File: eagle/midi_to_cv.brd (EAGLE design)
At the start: 100.1 x 82 mm, 67 parts, among them IC1 TL082P, IC2 TL084P, IC4 TL082P, IC6 TL082P, IC7 TL082P, U1 ATMEGA328P_PDIP, U2 MCP4822-E/P, U3 MCP4822-E/P, U4 MCP4822-E/P, U5 MCP4822-E/P

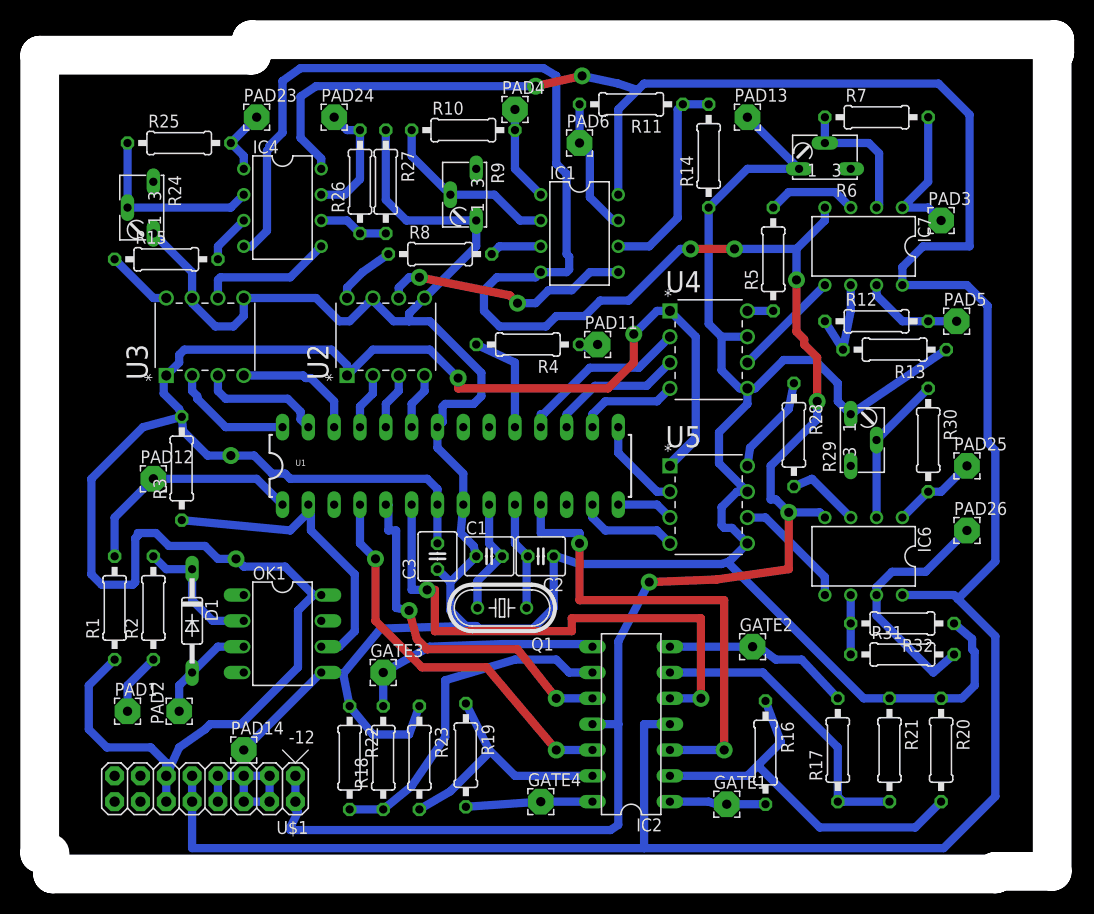
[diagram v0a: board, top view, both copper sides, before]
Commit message: updated arduino code
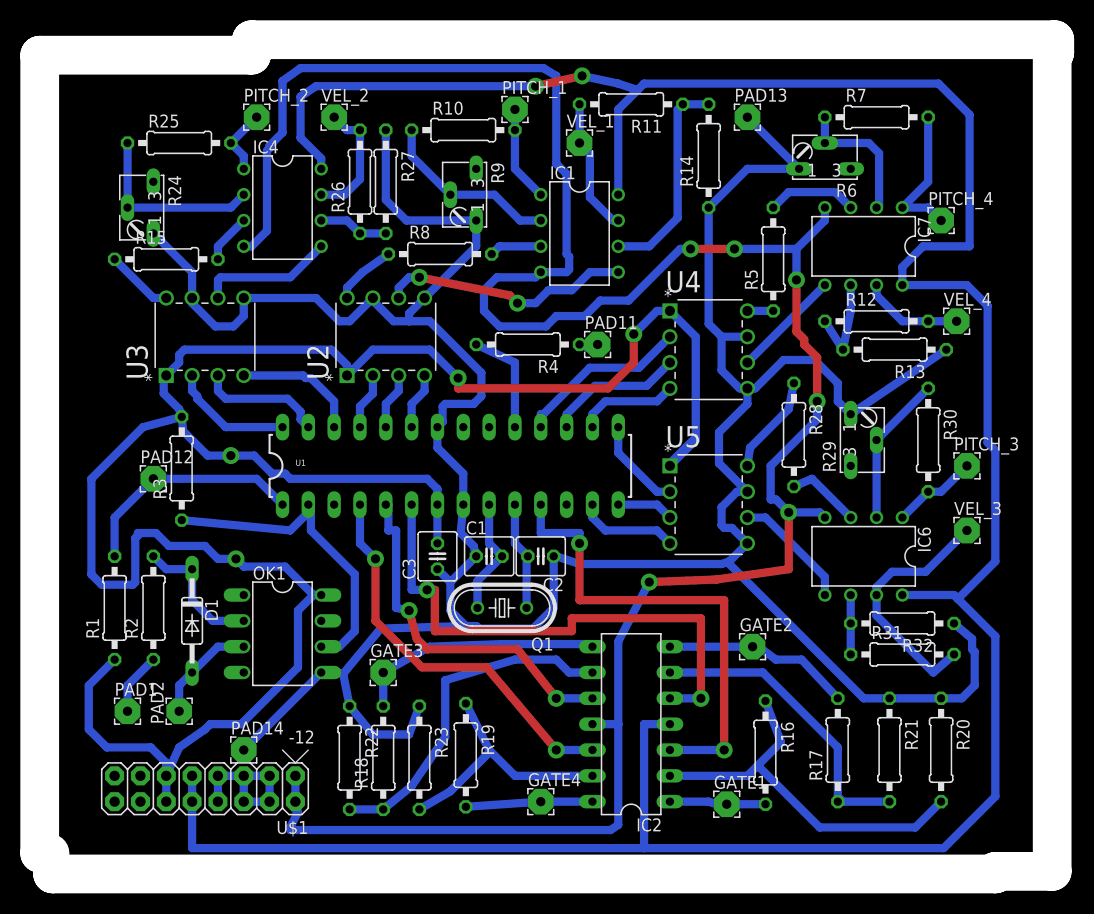
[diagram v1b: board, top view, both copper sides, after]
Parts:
- PITCH_1, PITCH_2, PITCH_3, PITCH_4: value pitch cv -> (none)
- VEL_1, VEL_2, VEL_3, VEL_4: value velocity cv -> (none)
- renumbered PAD23 to PITCH_2, PAD24 to VEL_2, PAD25 to PITCH_3, PAD26 to VEL_3, PAD3 to PITCH_4, PAD4 to PITCH_1, PAD5 to VEL_4, PAD6 to VEL_1
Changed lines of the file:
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@@
 <element name="R5" library="rcl" package="0207/10" value="3.3k" x="72.39" y="59.69" rot="R90"/>
 <element name="R6" library="pot" package="B64W" value="10k" x="77.47" y="68.58" rot="R180"/>
-<element name="PAD3" library="wirepad" package="2,54/0,9" value="pitch cv" x="88.9" y="63.5"/>
+<element name="PITCH_4" library="wirepad" package="2,54/0,9" value="" x="88.9" y="63.5"/>
 <element name="R7" library="rcl" package="0207/10" value="5k" x="82.55" y="73.66"/>
 <element name="R12" library="rcl" package="0207/10" value="1k" x="82.55" y="53.594"/>
 <element name="R13" library="rcl" package="0207/10" value="1k" x="84.328" y="50.8" rot="R180"/>
-<element name="PAD5" library="wirepad" package="2,54/0,9" value="velocity cv" x="90.424" y="53.594"/>
+<element name="VEL_4" library="wirepad" package="2,54/0,9" value="" x="90.424" y="53.594"/>
 <element name="U4" library="MCP4822" package="DIP254P762X432-8" value="MCP4822-E/P" x="69.85" y="46.99">
 <attribute name="PACKAGE" value="DIP-8" x="69.85" y="46.99" size="1.778" layer="27" display="off"/>
@@
 <element name="R8" library="rcl" package="0207/10" value="3.3k" x="39.624" y="60.198"/>
 <element name="R9" library="pot" package="B64W" value="10k" x="43.18" y="66.04" rot="R270"/>
-<element name="PAD4" library="wirepad" package="2,54/0,9" value="pitch cv" x="46.99" y="74.422"/>
+<element name="PITCH_1" library="wirepad" package="2,54/0,9" value="" x="46.99" y="74.422"/>
 <element name="R10" library="rcl" package="0207/10" value="5k" x="41.91" y="72.39"/>
 <element name="R11" library="rcl" package="0207/10" value="1k" x="58.42" y="74.93" rot="R180"/>
 <element name="R14" library="rcl" package="0207/10" value="1k" x="66.04" y="69.85" rot="R90"/>
-<element name="PAD6" library="wirepad" package="2,54/0,9" value="velocity cv" x="53.34" y="71.12"/>
+<element name="VEL_1" library="wirepad" package="2,54/0,9" value="" x="53.34" y="71.12"/>
 <element name="U2" library="MCP4822" package="DIP254P762X432-8" value="MCP4822-E/P" x="38.1" y="55.88" rot="R90">
 <attribute name="PACKAGE" value="DIP-8" x="72.39" y="41.91" size="1.778" layer="27" rot="R90" display="off"/>
@@
 <element name="R15" library="rcl" package="0207/10" value="3.3k" x="12.7" y="59.69"/>
 <element name="R24" library="pot" package="B64W" value="10k" x="11.43" y="64.77" rot="R270"/>
-<element name="PAD23" library="wirepad" package="2,54/0,9" value="pitch cv" x="21.59" y="73.66"/>
+<element name="PITCH_2" library="wirepad" package="2,54/0,9" value="" x="21.59" y="73.66"/>
 <element name="R25" library="rcl" package="0207/10" value="5k" x="13.97" y="71.12"/>
 <element name="R26" library="rcl" package="0207/10" value="1k" x="31.75" y="67.31" rot="R90"/>
 <element name="R27" library="rcl" package="0207/10" value="1k" x="34.29" y="67.31" rot="R270"/>
-<element name="PAD24" library="wirepad" package="2,54/0,9" value="velocity cv" x="29.21" y="73.66"/>
+<element name="VEL_2" library="wirepad" package="2,54/0,9" value="" x="29.21" y="73.66"/>
 <element name="U3" library="MCP4822" package="DIP254P762X432-8" value="MCP4822-E/P" x="20.32" y="55.88" rot="R90">
 <attribute name="PACKAGE" value="DIP-8" x="54.61" y="41.91" size="1.778" layer="27" rot="R90" display="off"/>
@@
 <element name="R28" library="rcl" package="0207/10" value="3.3k" x="74.422" y="42.418" rot="R270"/>
 <element name="R29" library="pot" package="B64W" value="10k" x="80.01" y="41.91" rot="R90"/>
-<element name="PAD25" library="wirepad" package="2,54/0,9" value="pitch cv" x="91.44" y="39.37"/>
+<element name="PITCH_3" library="wirepad" package="2,54/0,9" value="" x="91.44" y="39.37"/>
 <element name="R30" library="rcl" package="0207/10" value="5k" x="87.63" y="41.91" rot="R270"/>
 <element name="R31" library="rcl" package="0207/10" value="1k" x="85.09" y="20.828"/>
 <element name="R32" library="rcl" package="0207/10" value="1k" x="85.09" y="23.876" rot="R180"/>
-<element name="PAD26" library="wirepad" package="2,54/0,9" value="velocity cv" x="91.44" y="33.02"/>
+<element name="VEL_3" library="wirepad" package="2,54/0,9" value="" x="91.44" y="33.02"/>
 <element name="U5" library="MCP4822" package="DIP254P762X432-8" value="MCP4822-E/P" x="69.85" y="31.75">
 <attribute name="PACKAGE" value="DIP-8" x="55.88" y="-2.54" size="1.778" layer="27" display="off"/>
@@
 </signal>
 <signal name="N$9">
-<contactref element="PAD3" pad="1"/>
+<contactref element="PITCH_4" pad="1"/>
 <contactref element="R7" pad="2"/>
 <contactref element="IC7" pad="1"/>
@@
 <signal name="N$19">
 <contactref element="R12" pad="2"/>
-<contactref element="PAD5" pad="1"/>
+<contactref element="VEL_4" pad="1"/>
 <contactref element="IC7" pad="7"/>
 <wire x1="82.55" y1="57.15" x2="82.55" y2="56.134" width="0.8128" layer="16"/>
@@
 </signal>
 <signal name="N$17">
-<contactref element="PAD4" pad="1"/>
+<contactref element="PITCH_1" pad="1"/>
 <contactref element="R10" pad="2"/>
 <contactref element="IC1" pad="1"/>
@@
 <signal name="N$21">
 <contactref element="R11" pad="2"/>
-<contactref element="PAD6" pad="1"/>
+<contactref element="VEL_1" pad="1"/>
 <contactref element="IC1" pad="7"/>
 <wire x1="57.15" y1="63.5" x2="56.642" y2="63.5" width="0.8128" layer="16"/>
@@
 </signal>
 <signal name="N$49">
-<contactref element="PAD23" pad="1"/>
+<contactref element="PITCH_2" pad="1"/>
 <contactref element="R25" pad="2"/>
 <contactref element="IC4" pad="1"/>
@@
 <signal name="N$52">
 <contactref element="R26" pad="2"/>
-<contactref element="PAD24" pad="1"/>
+<contactref element="VEL_2" pad="1"/>
 <contactref element="IC4" pad="7"/>
 <wire x1="31.75" y1="72.39" x2="30.48" y2="72.39" width="0.8128" layer="16"/>
@@
 </signal>
 <signal name="N$57">
-<contactref element="PAD25" pad="1"/>
+<contactref element="PITCH_3" pad="1"/>
 <contactref element="R30" pad="2"/>
 <contactref element="IC6" pad="1"/>
@@
 <signal name="N$59">
 <contactref element="R31" pad="2"/>
-<contactref element="PAD26" pad="1"/>
+<contactref element="VEL_3" pad="1"/>
 <contactref element="IC6" pad="7"/>
 <wire x1="90.17" y1="20.828" x2="88.138" y2="19.05" width="0.8128" layer="16"/>
